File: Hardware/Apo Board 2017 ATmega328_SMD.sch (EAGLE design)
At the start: 29 parts, among them U1 LED-TRICOLOR-5050-IC, U10 LED-TRICOLOR-5050-IC, U11 LED-TRICOLOR-5050-IC, U2 ATMEGA328P_PDIP, U3 LED-TRICOLOR-5050-IC, U4 LED-TRICOLOR-5050-IC, U5 LED-TRICOLOR-5050-IC, U6 LED-TRICOLOR-5050-IC, U7 LED-TRICOLOR-5050-IC, U8 LED-TRICOLOR-5050-IC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

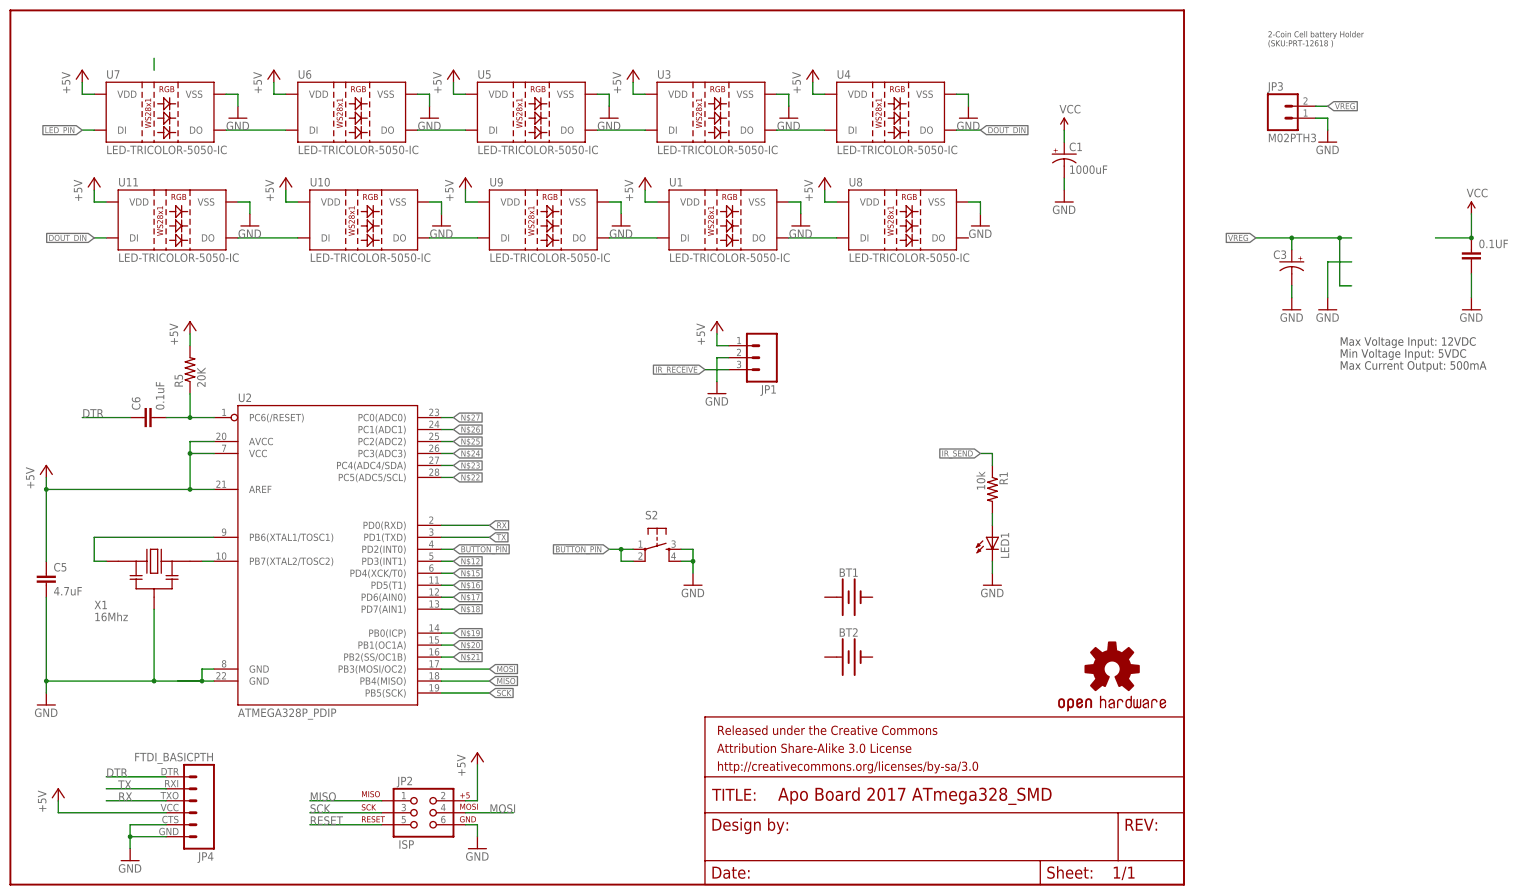
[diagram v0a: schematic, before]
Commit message: Adding ATmega328 versions
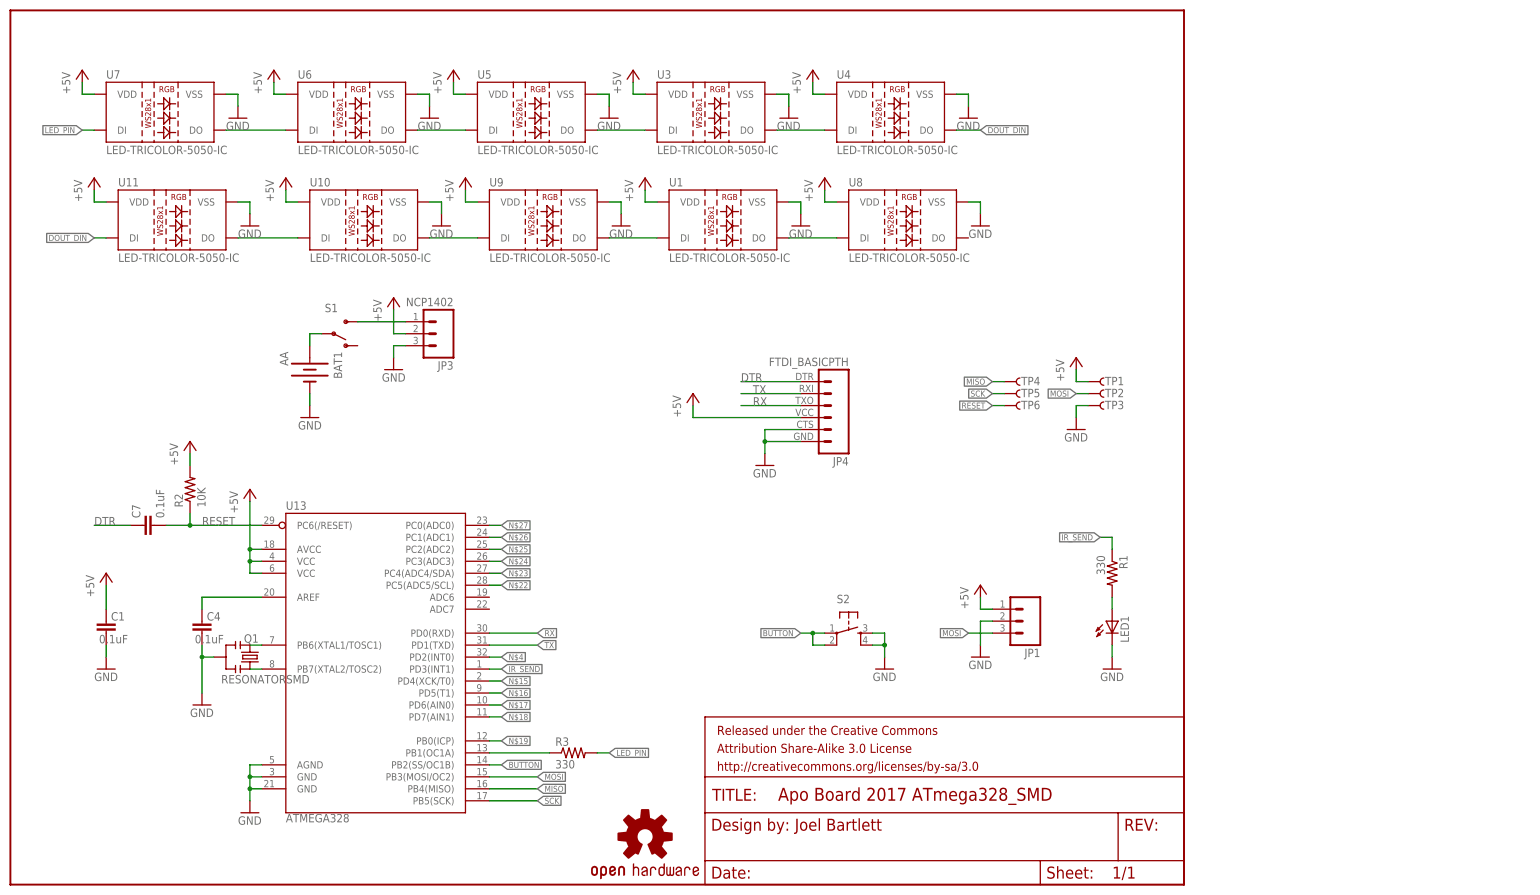
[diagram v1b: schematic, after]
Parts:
- removed 0.1UF: (no value), SparkFun-Capacitors:CAPKIT
- removed BT1, BT2: (no value), SparkFun-Batteries:BATTERY-AAA
- removed C3: (no value), SparkFun-Capacitors:CAP_POLPTH2
- removed C5: 4.7uF, SparkFun-Passives:CAPKIT
- removed C6: 0.1uF, SparkFun-Passives:CAPKIT
- removed JP2: ISP, SparkFun:AVR_SPI_PRG_6PTH
- removed R5: 20K, SparkFun-Passives:RESISTORKIT
- removed U2: ATMEGA328P_PDIP, SparkFun-DigitalIC:ATMEGA328P_PDIP
- removed X1: 16Mhz, 1_Dan Master:CERAMIC_RESONATOR
- added BAT1: AA, SparkFun:BATTERYAA-KIT
- added C4, C7: 0.1uF, SparkFun:CAP0402-CAP
- added Q1: RESONATORSMD, SparkFun:RESONATORSMD
- added R2: 10K, SparkFun:RESISTOR0402-RES
- added R3: 330, SparkFun-Resistors:RESISTORPTH-1/4W
- added S1: (no value), SparkFun:SWITCH-SPSTKIT
- added TP1, TP2, TP3, TP4, TP5, TP6: TP-3x5, SparkFun-Passives:TEST-POINT3X5
- added U13: ATMEGA328, SparkFun:ATMEGA168
- C1: value 1000uF -> 0.1uF; device SparkFun-Capacitors:CAP_POLPTH2 -> SparkFun:CAP0402-CAP
- JP1: device SparkFun-Connectors:M03PTH -> SparkFun-Connectors:M03IR_RECEIVER
- JP3: value M02PTH3 -> NCP1402; device SparkFun-Connectors:M02PTH3 -> SparkFun-Connectors:M03BOOST
- R1: value 10k -> 330
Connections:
- removed net BUTTON_PIN: S2.1, S2.2, U2.PD2(INT0)
- removed net IR_RECEIVE: JP1.3
- removed net N$10: C6.2, R5.1, U2.PC6(/RESET)
- removed net N$12: U2.PD3(INT1)
- removed net N$21: U2.PB2(SS/OC1B)
- removed net VCC: 0.1UF.1, C1.+
- removed net VREG: C3.+, JP3.2
- new net AREF: C4.2, U13.AREF
- new net BUTTON: S2.1, S2.2, U13.PB2(SS/OC1B)
- new net N$29: Q1.1, U13.PB7(XTAL2/TOSC2)
- new net N$30: Q1.3, U13.PB6(XTAL1/TOSC1)
- new net N$8: JP3.1, S1.S
- net +5V: now also C1.2, JP3.2, R2.2, TP1.1, U13.AVCC, U13.VCC@1, U13.VCC@2; no longer C5.1, JP2.2, R5.2, U2.AREF, U2.AVCC, U2.VCC
- net DTR: now also C7.1; no longer C6.1
- net GND: now also BAT1.-, C1.1, C4.1, JP3.3, Q1.2, TP3.1, U13.AGND, U13.GND@1, U13.GND@2; no longer 0.1UF.2, C1.-, C3.-, C5.2, JP2.6, JP3.1, U2.GND@1, U2.GND@2, X1.P$2
- net IR_SEND: now also U13.PD3(INT1)
- net LED_PIN: now also R3.2
- net MISO: now also TP4.1, U13.PB4(MISO); no longer JP2.1, U2.PB4(MISO)
- net MOSI: now also JP1.3, TP2.1, U13.PB3(MOSI/OC2); no longer JP2.4, U2.PB3(MOSI/OC2)
- net N$15: now also U13.PD4(XCK/T0); no longer U2.PD4(XCK/T0)
- net N$16: now also U13.PD5(T1); no longer U2.PD5(T1)
- net N$17: now also U13.PD6(AIN0); no longer U2.PD6(AIN0)
- net N$18: now also U13.PD7(AIN1); no longer U2.PD7(AIN1)
- net N$19: now also U13.PB0(ICP); no longer U2.PB0(ICP)
- net N$20: now also R3.1, U13.PB1(OC1A); no longer U2.PB1(OC1A)
- net N$22: now also U13.PC5(ADC5/SCL); no longer U2.PC5(ADC5/SCL)
- net N$23: now also U13.PC4(ADC4/SDA); no longer U2.PC4(ADC4/SDA)
- net N$24: now also U13.PC3(ADC3); no longer U2.PC3(ADC3)
- net N$25: now also U13.PC2(ADC2); no longer U2.PC2(ADC2)
- net N$26: now also U13.PC1(ADC1); no longer U2.PC1(ADC1)
- net N$27: now also U13.PC0(ADC0); no longer U2.PC0(ADC0)
- net N$4: now also U13.PD2(INT0); no longer U2.PB6(XTAL1/TOSC1), X1.P$1
- net N$7: now also BAT1.+, S1.P; no longer U2.PB7(XTAL2/TOSC2), X1.P$3
- net RESET: now also C7.2, R2.1, TP6.1, U13.PC6(/RESET); no longer JP2.5
- net RX: now also U13.PD0(RXD); no longer U2.PD0(RXD)
- net SCK: now also TP5.1, U13.PB5(SCK); no longer JP2.3, U2.PB5(SCK)
- net TX: now also U13.PD1(TXD); no longer U2.PD1(TXD)
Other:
- note added: "Joel Bartlett"
- note removed: "2-Coin Cell battery Holder (SKU:PRT-12618 )"
- note removed: "Max Current Output: 500mA"
- note removed: "Max Voltage Input: 12VDC"
- note removed: "Min Voltage Input: 5VDC"
- moved on the sheet: JP1, JP4, LED1, R1, S2

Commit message: Cleanup
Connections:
- net GND: now also JP3.1; no longer JP3.3
- net N$8: now also JP3.3; no longer JP3.1
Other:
- moved on the sheet: JP3
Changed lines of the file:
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@@
 <instance part="S1" gate="1" x="68.58" y="116.84" rot="MR180"/>
 <instance part="BAT1" gate="G$1" x="63.5" y="109.22" rot="R270"/>
-<instance part="JP3" gate="G$1" x="91.44" y="116.84" rot="R180"/>
-<instance part="GND7" gate="1" x="81.28" y="109.22" rot="MR0"/>
-<instance part="P+16" gate="1" x="81.28" y="124.46"/>
+<instance part="JP3" gate="G$1" x="91.44" y="121.92" rot="R180"/>
+<instance part="GND7" gate="1" x="83.82" y="114.3" rot="MR0"/>
+<instance part="P+16" gate="1" x="81.28" y="127"/>
 <instance part="R3" gate="G$1" x="119.38" y="27.94"/>
 <instance part="C1" gate="G$1" x="20.32" y="55.88" smashed="yes" rot="R180">
@@
 </segment>
 <segment>
-<pinref part="JP3" gate="G$1" pin="3"/>
-<pinref part="GND7" gate="1" pin="GND"/>
-<wire x1="83.82" y1="114.3" x2="81.28" y2="114.3" width="0.1524" layer="91"/>
-<wire x1="81.28" y1="114.3" x2="81.28" y2="111.76" width="0.1524" layer="91"/>
-</segment>
-<segment>
 <pinref part="C1" gate="G$1" pin="1"/>
 <pinref part="GND9" gate="1" pin="GND"/>
@@
 <pinref part="GND27" gate="1" pin="GND"/>
 <wire x1="226.06" y1="99.06" x2="226.06" y2="101.6" width="0.1524" layer="91"/>
+</segment>
+<segment>
+<pinref part="JP3" gate="G$1" pin="1"/>
+<wire x1="83.82" y1="124.46" x2="83.82" y2="116.84" width="0.1524" layer="91"/>
+<pinref part="GND7" gate="1" pin="GND"/>
 </segment>
 </net>
@@
 <pinref part="JP3" gate="G$1" pin="2"/>
 <pinref part="P+16" gate="1" pin="+5V"/>
-<wire x1="83.82" y1="116.84" x2="81.28" y2="116.84" width="0.1524" layer="91"/>
-<wire x1="81.28" y1="116.84" x2="81.28" y2="121.92" width="0.1524" layer="91"/>
+<wire x1="83.82" y1="121.92" x2="81.28" y2="121.92" width="0.1524" layer="91"/>
+<wire x1="81.28" y1="121.92" x2="81.28" y2="124.46" width="0.1524" layer="91"/>
 </segment>
 <segment>
@@
 </segment>
 </net>
-<net name="N$8" class="0">
-<segment>
-<pinref part="S1" gate="1" pin="S"/>
-<pinref part="JP3" gate="G$1" pin="1"/>
-<wire x1="73.66" y1="119.38" x2="83.82" y2="119.38" width="0.1524" layer="91"/>
-</segment>
-</net>
 <net name="N$4" class="0">
 <segment>
@@
 </segment>
 </net>
+<net name="N$8" class="0">
+<segment>
+<pinref part="JP3" gate="G$1" pin="3"/>
+<pinref part="S1" gate="1" pin="S"/>
+<wire x1="83.82" y1="119.38" x2="73.66" y2="119.38" width="0.1524" layer="91"/>
+</segment>
+</net>

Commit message: Power Tests
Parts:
- added BAT2: AA, SparkFun:BATTERYAA-KIT
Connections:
- new net N$10: BAT1.+, BAT2.-
- net N$7: now also BAT2.+; no longer BAT1.+
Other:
- moved on the sheet: BAT1
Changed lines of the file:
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@@
 <?xml version="1.0" encoding="utf-8"?>
 <!DOCTYPE eagle SYSTEM "eagle.dtd">
-<eagle version="7.3.0">
+<eagle version="7.6.0">
 <drawing>
 <settings>
@@
 <part name="TP6" library="SparkFun-Passives" deviceset="TEST-POINT" device="3X5" value="TP-3x5"/>
 <part name="P+18" library="supply1" deviceset="+5V" device=""/>
+<part name="BAT2" library="SparkFun" deviceset="BATTERY" device="AA-KIT" value="AA"/>
 </parts>
 <sheets>
@@
 <instance part="GND38" gate="1" x="50.8" y="15.24"/>
 <instance part="P+1" gate="1" x="50.8" y="83.82"/>
-<instance part="GND22" gate="1" x="63.5" y="99.06" rot="MR0"/>
+<instance part="GND22" gate="1" x="35.56" y="111.76" rot="MR0"/>
 <instance part="S1" gate="1" x="68.58" y="116.84" rot="MR180"/>
-<instance part="BAT1" gate="G$1" x="63.5" y="109.22" rot="R270"/>
+<instance part="BAT1" gate="G$1" x="43.18" y="116.84" rot="R180"/>
 <instance part="JP3" gate="G$1" x="91.44" y="121.92" rot="R180"/>
 <instance part="GND7" gate="1" x="83.82" y="114.3" rot="MR0"/>
@@
 </instance>
 <instance part="P+18" gate="1" x="226.06" y="111.76"/>
+<instance part="BAT2" gate="G$1" x="55.88" y="116.84" rot="R180"/>
 </instances>
 <busses>
@@
 </segment>
 <segment>
-<wire x1="63.5" y1="101.6" x2="63.5" y2="104.14" width="0.1524" layer="91"/>
-<pinref part="GND22" gate="1" pin="GND"/>
-<pinref part="BAT1" gate="G$1" pin="-"/>
-</segment>
-<segment>
 <pinref part="C1" gate="G$1" pin="1"/>
 <pinref part="GND9" gate="1" pin="GND"/>
@@
 <wire x1="83.82" y1="124.46" x2="83.82" y2="116.84" width="0.1524" layer="91"/>
 <pinref part="GND7" gate="1" pin="GND"/>
+</segment>
+<segment>
+<pinref part="BAT1" gate="G$1" pin="-"/>
+<pinref part="GND22" gate="1" pin="GND"/>
+<wire x1="38.1" y1="116.84" x2="35.56" y2="116.84" width="0.1524" layer="91"/>
+<wire x1="35.56" y1="116.84" x2="35.56" y2="114.3" width="0.1524" layer="91"/>
 </segment>
 </net>
@@
 </segment>
 </net>
-<net name="N$7" class="0">
-<segment>
-<wire x1="63.5" y1="114.3" x2="63.5" y2="116.84" width="0.1524" layer="91"/>
-<wire x1="63.5" y1="116.84" x2="66.04" y2="116.84" width="0.1524" layer="91"/>
-<pinref part="S1" gate="1" pin="P"/>
-<pinref part="BAT1" gate="G$1" pin="+"/>
-</segment>
-</net>
 <net name="N$4" class="0">
 <segment>
@@
 </segment>
 </net>
+<net name="N$7" class="0">
+<segment>
+<pinref part="S1" gate="1" pin="P"/>
+<pinref part="BAT2" gate="G$1" pin="+"/>
+<wire x1="60.96" y1="116.84" x2="66.04" y2="116.84" width="0.1524" layer="91"/>
+</segment>
+</net>
+<net name="N$10" class="0">
+<segment>
+<pinref part="BAT2" gate="G$1" pin="-"/>
+<pinref part="BAT1" gate="G$1" pin="+"/>
+<wire x1="48.26" y1="116.84" x2="50.8" y2="116.84" width="0.1524" layer="91"/>
+</segment>
+</net>
